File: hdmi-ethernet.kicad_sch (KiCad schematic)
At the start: 121 parts, among them J15 0895-2C1R-GVH, J16 2007435-1, U26 LAN8720A-CP-TR-ABC, U27 KSZ9131RNXC, U28 TPD4E05U06QDQARQ1, U29 TPD4E05U06QDQARQ1, Y3 ABM8G-25.000MHZ-18-D2Y-T, Y4 ABM8G-25.000MHZ-18-D2Y-T

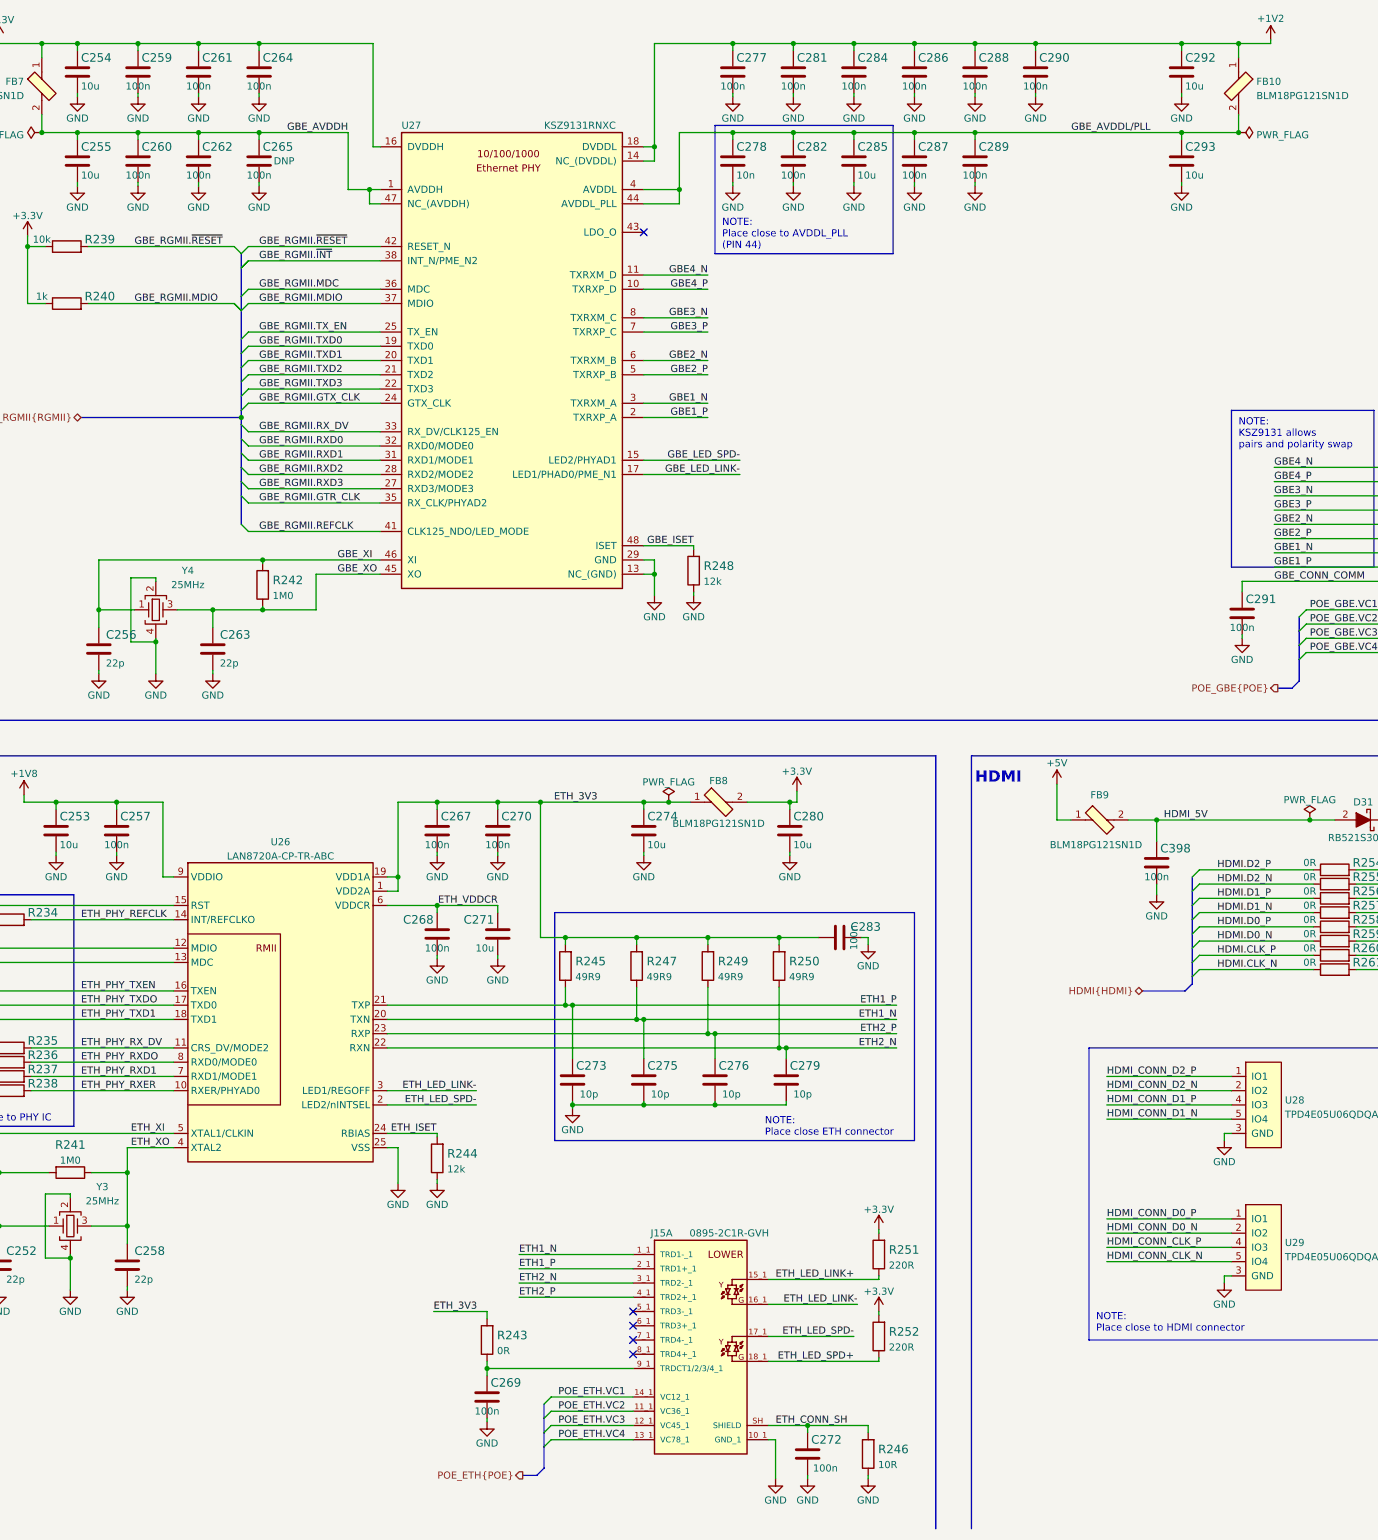
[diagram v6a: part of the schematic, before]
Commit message: Fix 100n value position
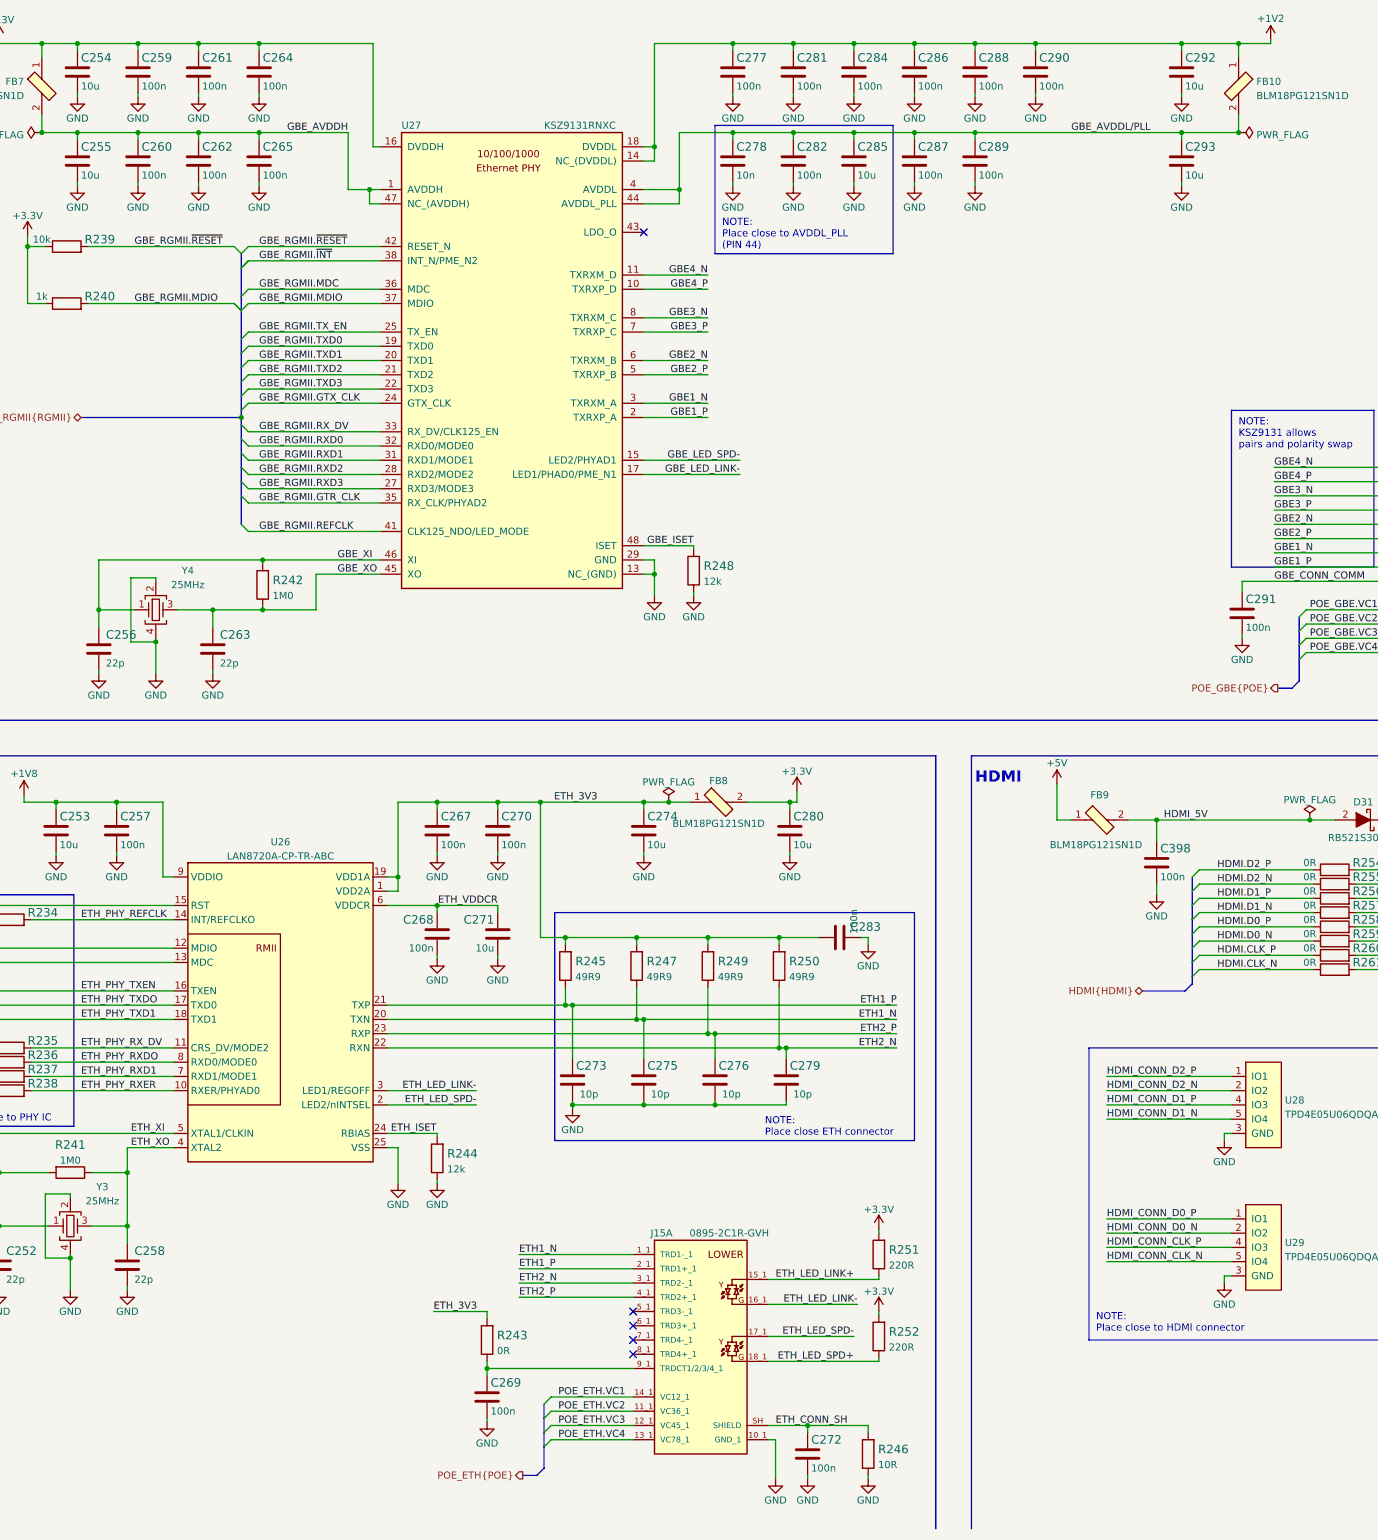
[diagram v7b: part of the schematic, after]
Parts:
- C265: DNP DNP -> (none)

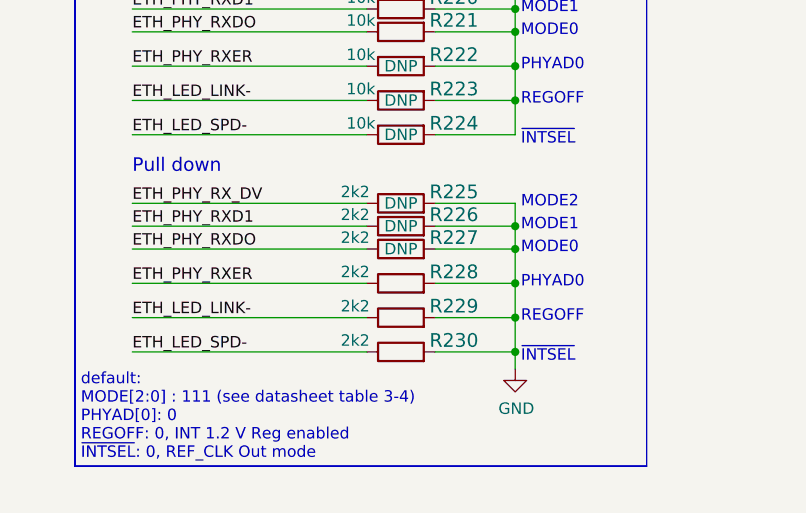
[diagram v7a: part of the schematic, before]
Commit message: Corrected schematic according to review
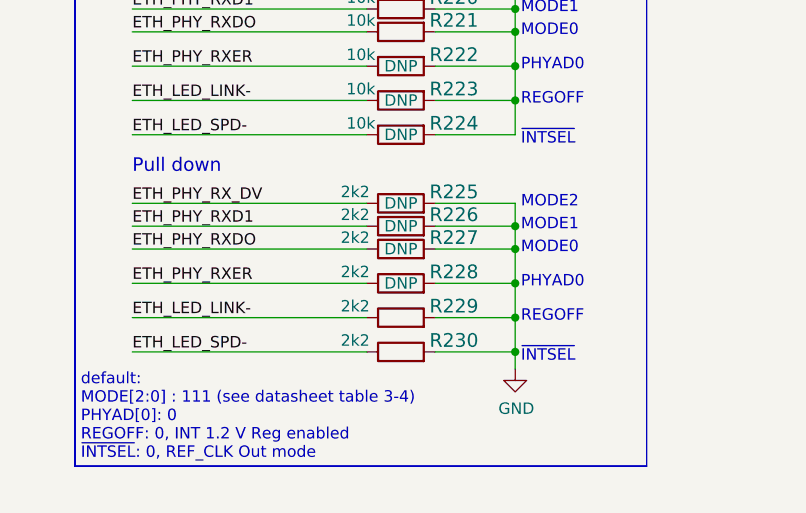
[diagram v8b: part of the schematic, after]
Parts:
- R228: DNP (none) -> DNP
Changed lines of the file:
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@@
     )
     (property "Val" "2k2" (id 6) (at 50.165 259.08 0))
+    (property "DNP" "DNP" (id 7) (at 55.245 260.35 0))
     (pin "1")
     (pin "2")
